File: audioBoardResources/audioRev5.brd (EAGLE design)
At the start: 88.9 x 71.1 mm, 60 parts, among them IC1 MCP604P, IC2 78L05Z, J9 AUDIO_JACK_3.5MM, Q1 FQP27P06, T1 TIP 31, T2 TIP 32, T3 2N3904, T4 2N3904

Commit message: Update boards to include QR code
Updated the board files for legacy EAGLE and current Fusion
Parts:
- moved C10 12.7 mm to (22.9, 35.6)
- moved C12 7.62 mm to (16.5, 35.6)
- moved C11 3.81 mm to (22.9, 42.5)
- moved C13 2.54 mm to (10.8, 36.2)
- moved D2 2.54 mm to (6.35, 38.7)
- moved R11 2.54 mm to (2.54, 38.7)
- moved C7 1.27 mm to (35.6, 49.5)
- moved IC2 1.27 mm to (26.7, 49.5)
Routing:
- net 2.5V: track 117.4 -> 113.2 mm
- net +5V: track 6.77 -> 7.51 mm

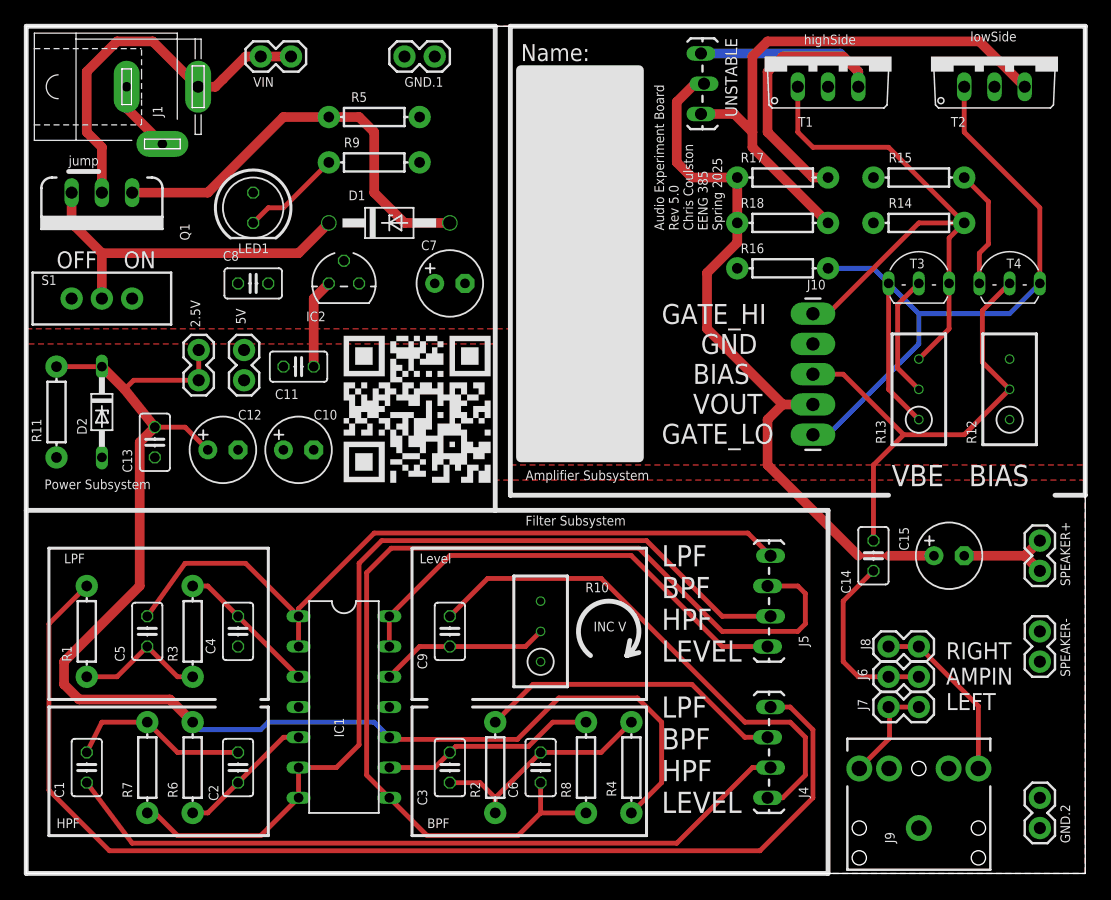
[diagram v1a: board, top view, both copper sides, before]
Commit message: update audioBoard to correct and latest version
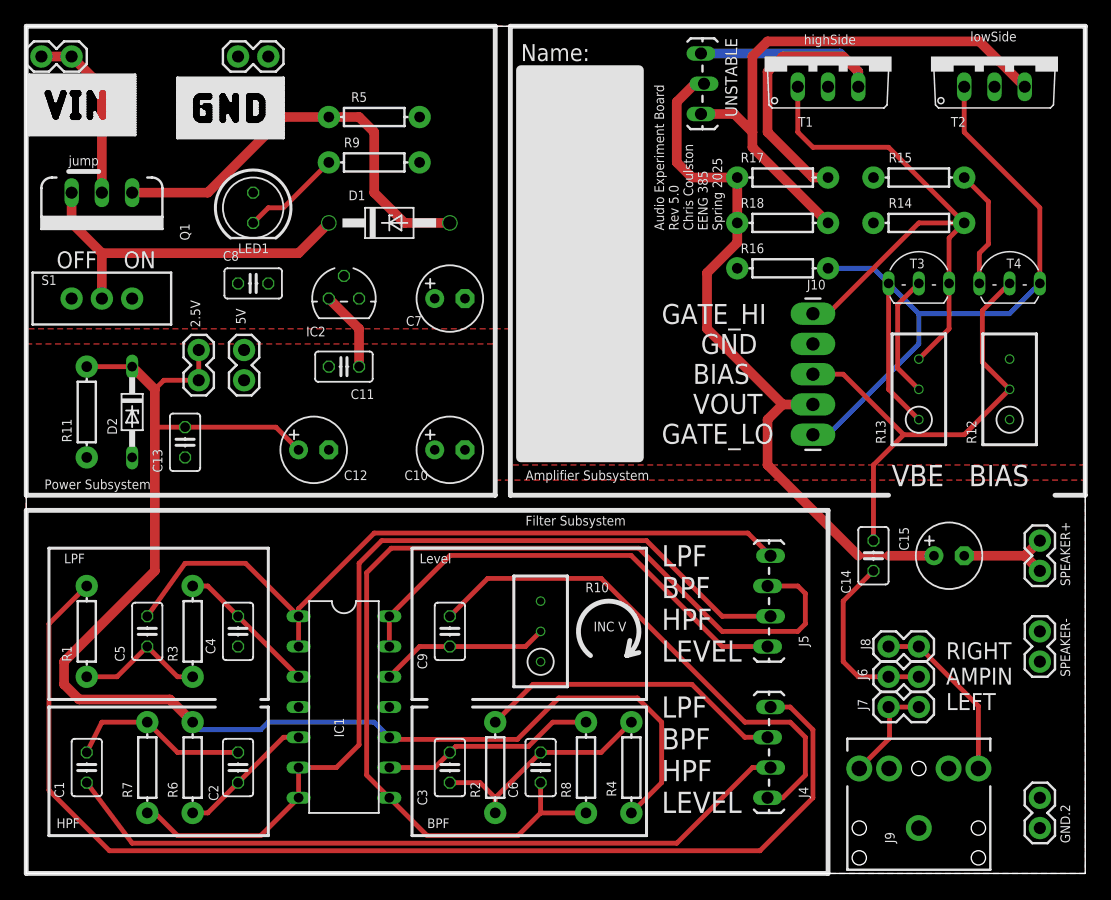
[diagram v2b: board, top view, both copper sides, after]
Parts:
- removed J1: (no value), con-jack:SPC4077
- R16: value 1k -> 33k
- moved VIN 18.4 mm to (3.81, 68.6)
- moved GND.1 14.0 mm to (20.3, 68.6)
- moved C10 12.7 mm to (35.6, 35.6)
- moved C12 7.62 mm to (24.1, 35.6)
- moved C11 3.81 mm to (26.7, 42.5)
- moved C13 2.54 mm to (13.3, 36.2)
- moved D2 2.54 mm to (8.89, 38.7)
- moved R11 2.54 mm to (5.08, 38.7)
- moved C7 1.27 mm to (35.6, 48.3)
- moved IC2 1.27 mm to (26.7, 48.3)
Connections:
- removed net DRAIN: J1.3, Q1.2, VIN.1, VIN.2
- new net VIN: Q1.2, VIN.1, VIN.2
- net GND: no longer J1.1, J1.2
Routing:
- net DRAIN: track 31.5 -> 0.00 mm
- net VIN: track 0.00 -> 15.0 mm
- net GND: track 6.04 -> 0.00 mm
- net 2.5V: track 113.2 -> 117.4 mm
- net +5V: track 7.51 -> 6.77 mm
